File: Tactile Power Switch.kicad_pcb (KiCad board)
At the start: 2 copper layers, 22 x 26 mm, 18 parts, among them J1 OSTTC020162, J2 OSTTC020162, Q1 BC847B_215, Q2 BC847B_215, Q4 NDT2955, SW1 SW_SPST

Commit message: mfg file initiated
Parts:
- removed D1: GREEN, LED_SMD:LED_0603_1608Metric
- removed REF**: OSHW-Symbol_6.7x6mm_SilkScreen, Symbol:OSHW-Symbol_6.7x6mm_SilkScreen
- removed SW1: SW_SPST, Button_Switch_SMD:SW_SPST_TL3342
- added S1: TSD1265, SW_TSD1265:SW_TSD1265, F.Cu at (120.0, 59.0)
- C1, C2, Q1, Q2, Q4, R1, R2, R3, R4: moved to B.Cu
- G***: moved to F.Cu
- moved R4 16.2 mm to (120.2, 69.5), turned to -90 degrees
- moved G*** 15.2 mm to (125.0, 69.0), turned to 0 degrees
- moved R2 14.5 mm to (121.8, 69.5)
- moved R1 10.8 mm to (130.4, 61.2)
- moved G*** 9.65 mm to (120.2, 59.0)
- moved R3 9.05 mm to (128.8, 61.2), turned to -90 degrees
- moved Q1 6.07 mm to (129.4, 65.2), turned to 180 degrees
- moved C1 3.65 mm to (125.0, 68.4)
- moved C2 3.48 mm to (125.0, 70.4), turned to 0 degrees
- moved Q4 3.40 mm to (113.8, 68.4)
- moved J1 3.13 mm to (115.0, 48.0)
- moved Q2 3.08 mm to (125.7, 65.2), turned to 180 degrees
- moved J2 2.67 mm to (122.4, 48.0)
- moved H1 2.24 mm to (129.5, 71.5)
- moved H2 2.24 mm to (110.5, 46.5)
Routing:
- net +12V: track 32.7 -> 51.5 mm
- net Net-(Q1-C): track 14.8 -> 32.7 mm, vias 2 -> 0
- net Net-(Q1-B): track 19.3 -> 36.5 mm, vias 0 -> 1
- net Net-(Q2-C): track 23.2 -> 25.8 mm, vias 0 -> 1
- net Net-(R4-Pad1): track 4.16 -> 2.74 mm
- net VDD: track 39.9 -> 38.8 mm
- net GND: track 6.21 -> 7.20 mm, vias 5 -> 4
- added copper zone on F.Cu, net GND
- removed copper zone on B.Cu, net GND
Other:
- board size 22 x 26 mm -> 24 x 30 mm
- board text added: "Tactile ON / OFF Power Switch THT version rev. 01"
- board text removed: "SMD VERSION REV.01"
- board text removed: "Tactile ON/OFF Power Button"

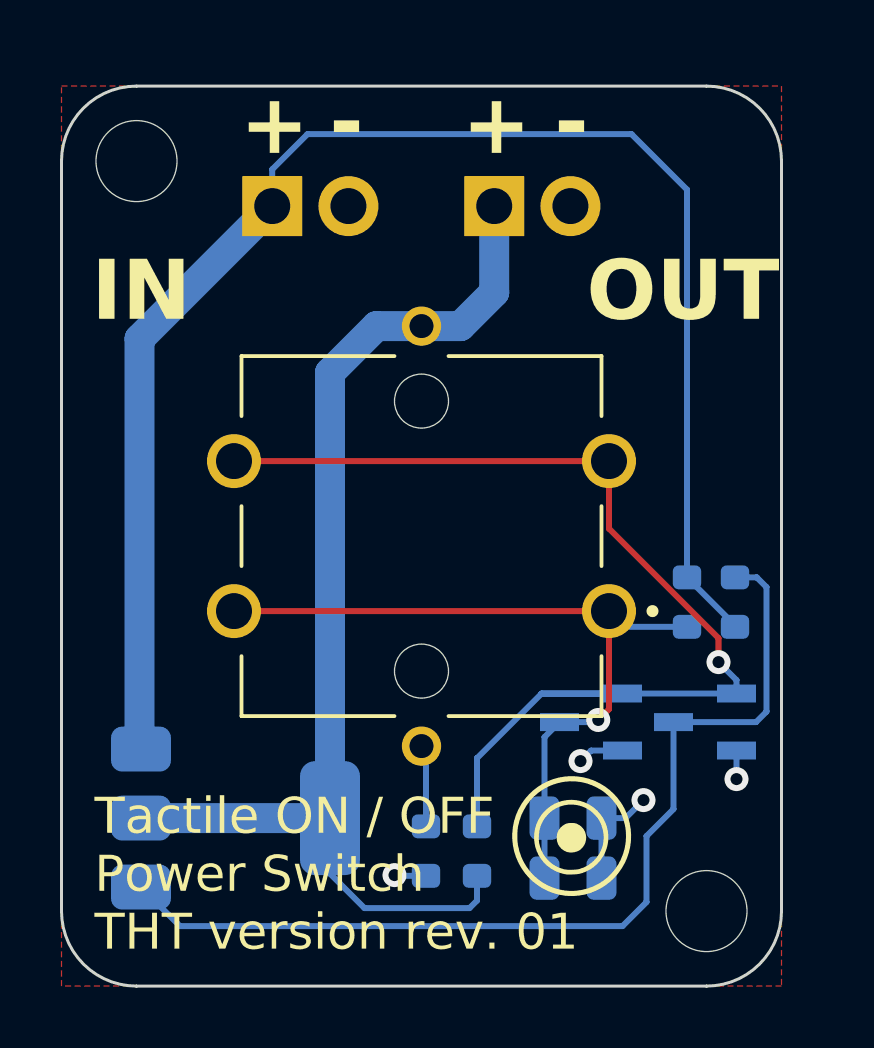
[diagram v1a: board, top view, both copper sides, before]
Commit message: smd version restored + mfg file created
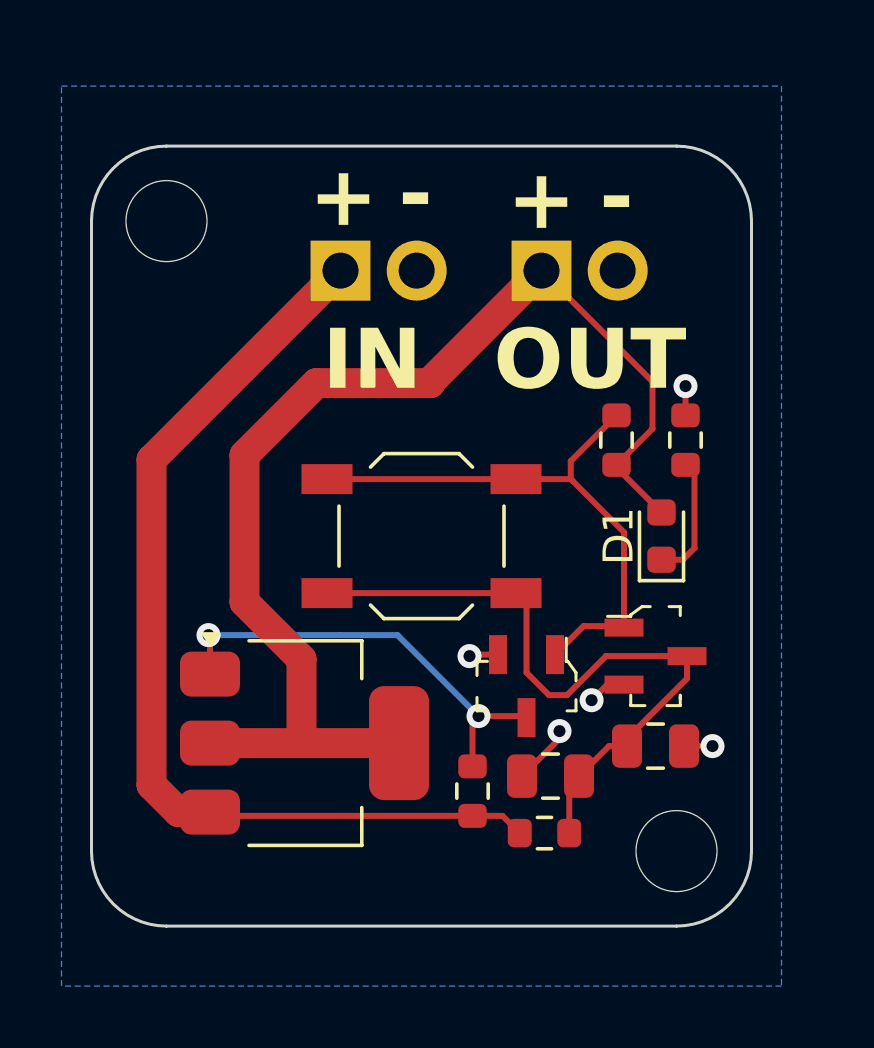
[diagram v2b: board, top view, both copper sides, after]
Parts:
- removed S1: TSD1265, SW_TSD1265:SW_TSD1265
- added D1: GREEN, LED_SMD:LED_0603_1608Metric, F.Cu at (128.0, 59.0)
- added REF**: OSHW-Symbol_6.7x6mm_SilkScreen, Symbol:OSHW-Symbol_6.7x6mm_SilkScreen, B.Cu at (114.1, 68.3)
- added SW1: SW_SPST, Button_Switch_SMD:SW_SPST_TL3342, F.Cu at (120.0, 59.0)
- C1, C2, Q1, Q2, Q4, R1, R2, R3, R4: moved to F.Cu
- G***: moved to B.Cu
- moved R4 16.2 mm to (128.8, 55.8), turned to 90 degrees
- moved G*** 15.2 mm to (111.5, 62.0), turned to 180 degrees
- moved R2 14.5 mm to (126.5, 55.8)
- moved R1 10.8 mm to (121.7, 67.5)
- moved G*** 9.65 mm to (122.4, 68.4)
- moved R3 9.05 mm to (124.1, 68.9), turned to 0 degrees
- moved Q1 6.07 mm to (123.5, 64.0), turned to -90 degrees
- moved C1 3.65 mm to (127.8, 66.0)
- moved C2 3.48 mm to (124.3, 67.0), turned to 180 degrees
- moved Q4 3.40 mm to (116.1, 65.9)
- moved J1 3.13 mm to (117.3, 50.1)
- moved Q2 3.08 mm to (127.8, 63.0), turned to 0 degrees
- moved J2 2.67 mm to (124.0, 50.1)
- moved H1 2.24 mm to (128.5, 69.5)
- moved H2 2.24 mm to (111.5, 48.5)
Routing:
- net +12V: track 51.5 -> 32.7 mm
- net Net-(Q1-C): track 32.7 -> 14.8 mm, vias 0 -> 2
- net Net-(Q1-B): track 36.5 -> 19.3 mm, vias 1 -> 0
- net Net-(Q2-C): track 25.8 -> 23.2 mm, vias 1 -> 0
- net Net-(D1-K): track 2.74 -> 4.16 mm
- net VDD: track 38.8 -> 39.9 mm
- net GND: track 7.20 -> 6.21 mm, vias 4 -> 5
- added copper zone on B.Cu, net GND
- removed copper zone on F.Cu, net GND
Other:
- board size 24 x 30 mm -> 22 x 26 mm
- board text added: "SMD VERSION REV.01"
- board text added: "Tactile ON/OFF Power Button"
- board text removed: "Tactile ON / OFF Power Switch THT version rev. 01"
